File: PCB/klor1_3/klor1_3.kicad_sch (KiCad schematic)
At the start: 88 parts, among them J1 MJ-4PP-9, J2 Haptic Buzz, J3 lv27, SW1 SW_PUSH-MX_W_LED, SW10 SW_PUSH-MX_W_LED, SW11 SW_PUSH-MX_W_LED, SW12 SW_PUSH-MX_W_LED, SW13 SW_PUSH-MX_W_LED, SW14 SW_PUSH-MX_W_LED, SW15 SW_PUSH-MX_W_LED, SW16 SW_PUSH-MX_W_LED, SW17 SW_PUSH-MX_W_LED, SW18 RotaryEncoder_Switch, SW19 SW_PUSH-MX_W_LED, SW2 SW_PUSH-MX_W_LED, SW20 SW_PUSH-MX_W_LED, SW21 SW_PUSH-MX_W_LED, SW22 SW_PUSH-MX_W_LED, SW3 SW_PUSH-MX_W_LED, SW4 SW_PUSH-MX_W_LED, SW5 SW_PUSH-MX_W_LED, SW6 SW_PUSH-MX_W_LED, SW7 SW_PUSH-MX_W_LED, SW8 SW_PUSH-MX_W_LED, SW9 SW_PUSH-MX_W_LED, U1 ProMicro

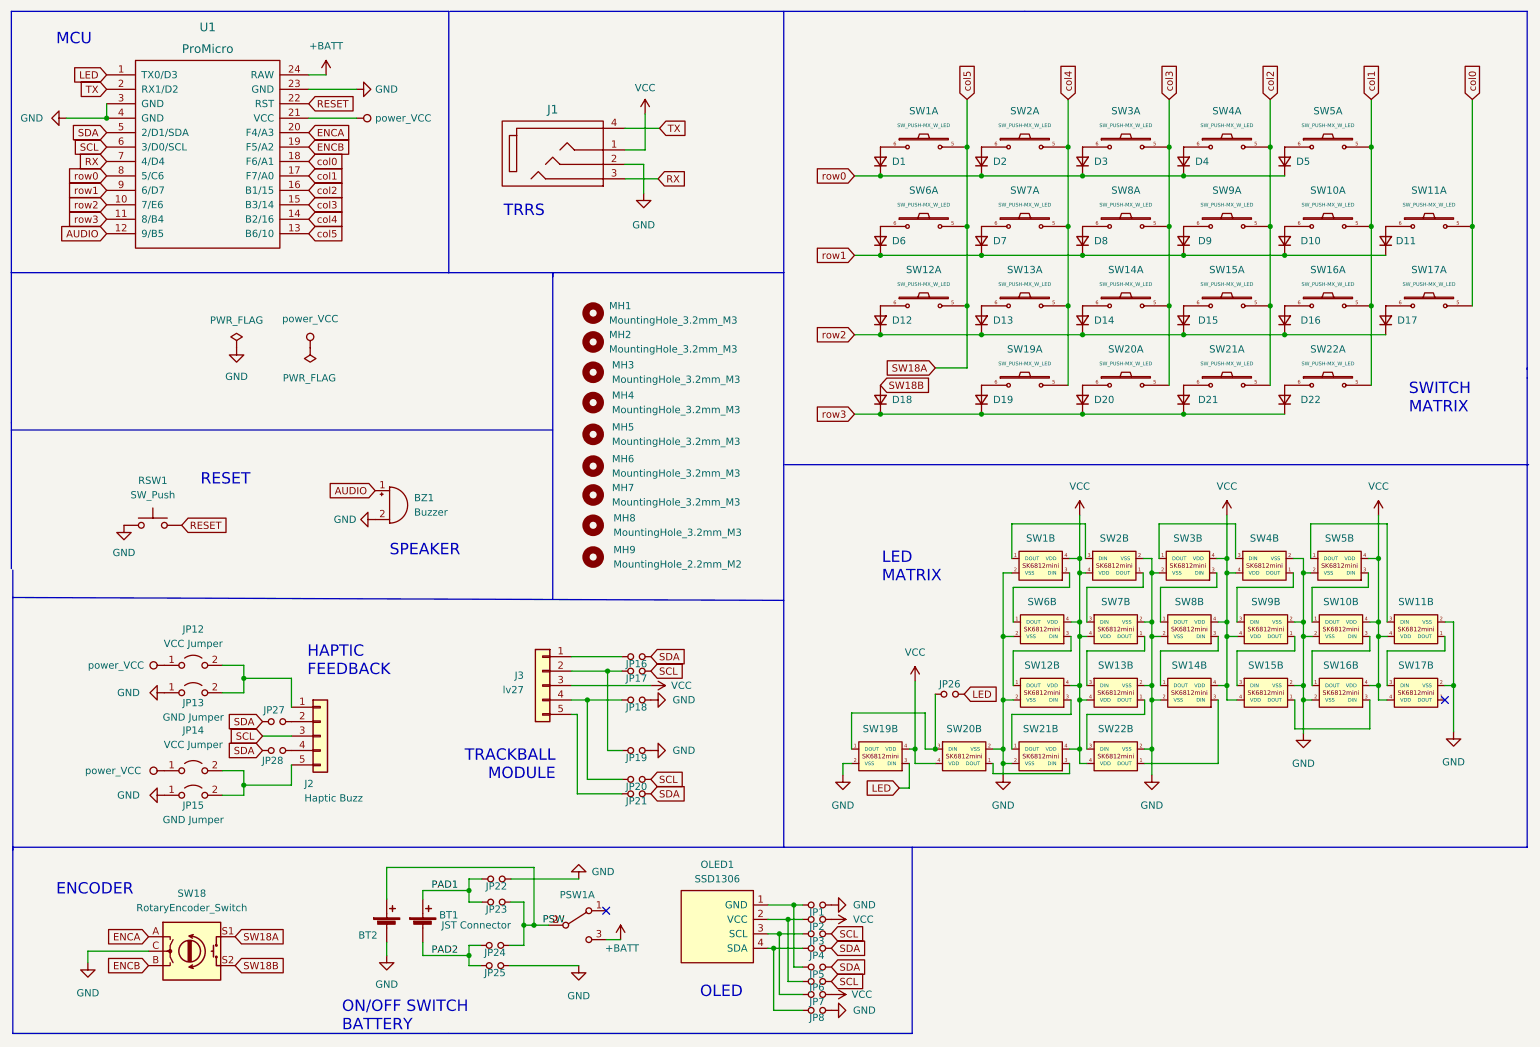
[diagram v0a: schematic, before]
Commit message: update schematic with 5way switch
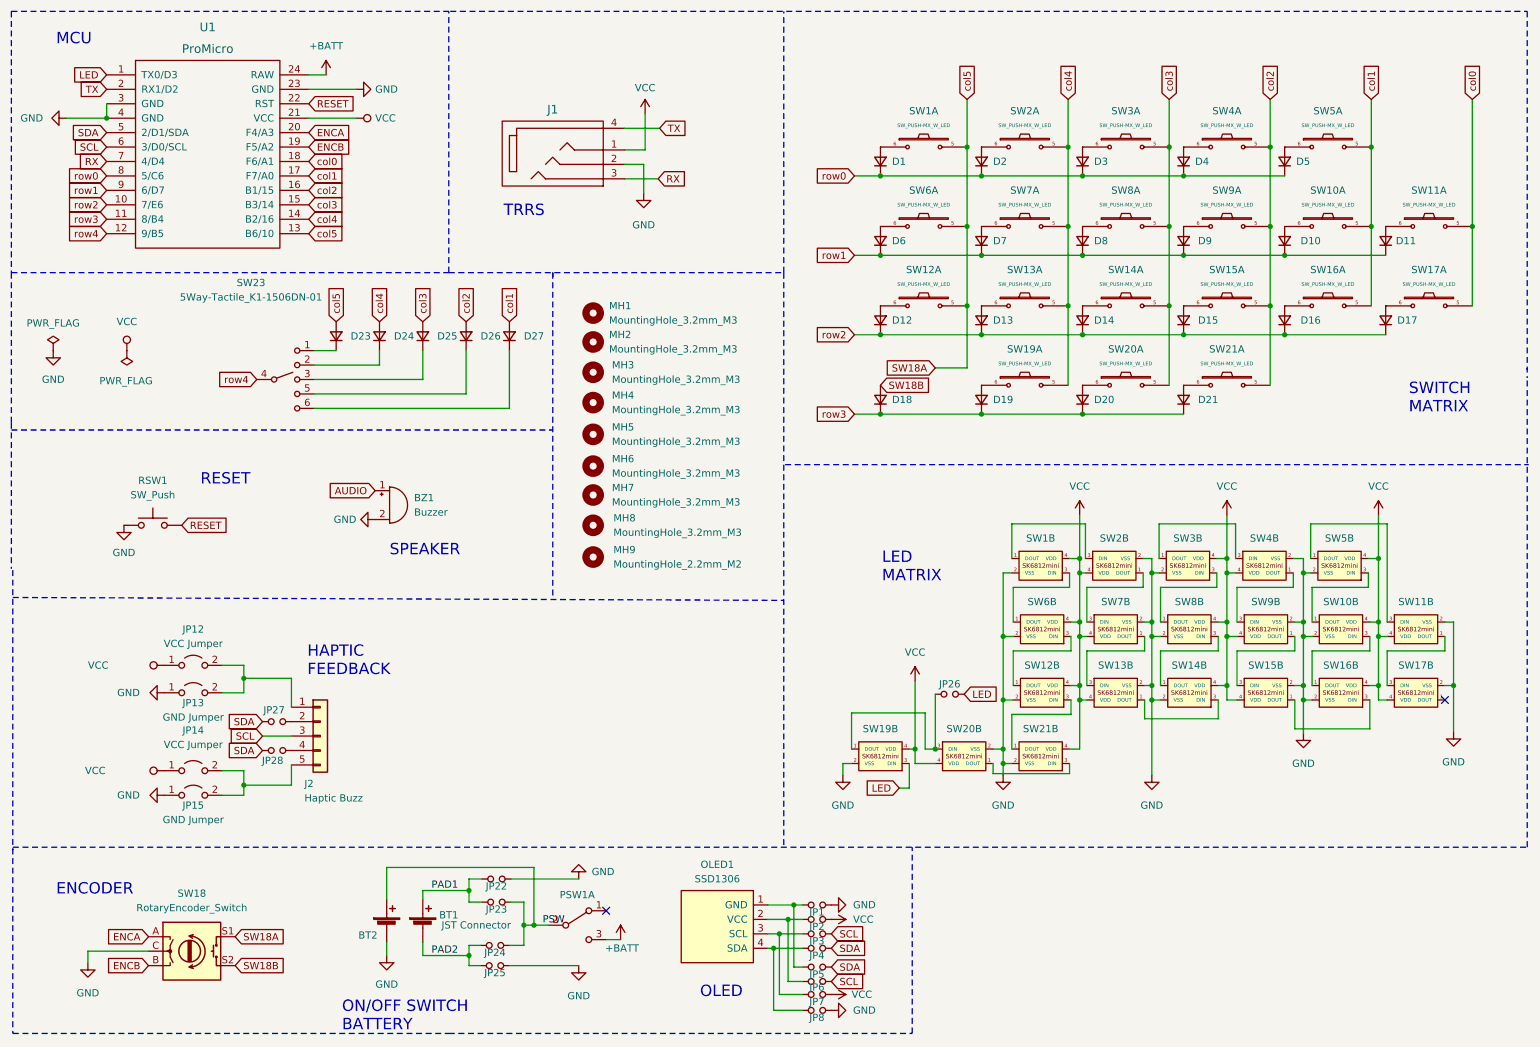
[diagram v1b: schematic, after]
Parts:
- removed D22: D_Small, KLOR:Diode_SOD123, symbol Device:D_Small
- removed J3: lv27, KLOR:lvc27_onlyInput, symbol Connector_Generic:Conn_01x05
- removed JP16, JP17, JP18, JP19, JP21: Device_Jumper_NO_Small, KLOR:Jumper, symbol KLORlib:Device_Jumper_NO_Small
- removed JP20: Device_Jumper_NO_Small, KLOR:Jumper, symbol SofleKeyboard-cache:Device_Jumper_NO_Small
- removed SW22: SW_PUSH-MX_W_LED, KLOR:SK6812MINI_and_cherry, symbol KLORlib:SW_PUSH-MX_W_LED
- added D23, D24, D25, D26, D27: D_Small, KLOR:Diode_SOD123, symbol Device:D_Small
- added SW23: 5Way-Tactile_K1-1506DN-01, reversible-kicad-footprints:5Way-K1-1506DN-01, symbol DjinnSymbols:5Way-Tactile_K1-1506DN-01
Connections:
- net AUDIO: no longer U1.12 (9/B5)
- net SW18A: now also D23.2 (A)
- net col1: now also D27.2 (A)
- net col2: now also D26.2 (A)
- net col3: now also D25.2 (A)
- net col4: now also D24.2 (A)
- net at SW14.3 (DIN): now also SW13.1 (DOUT)
- new net: D25.1 (K), SW23.3
- new net: D26.1 (K), SW23.5
- new net: D27.1 (K), SW23.6
- new net: D23.1 (K), SW23.1
- new net: D24.1 (K), SW23.2
- new net row4: SW23.4, U1.12 (9/B5)
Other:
- note removed: "TRACKBALL MODULE"
